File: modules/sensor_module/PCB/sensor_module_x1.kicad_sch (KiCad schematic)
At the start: 61 parts, among them J1 Screw_Terminal_01x02, J2 Conn_01x06_Socket, J3 Conn_01x03_Socket, SW1 SW_SPDT, U1 LM393, U2 MQ-5, U3 AMS1117-3.3, U4 AMS1117-5, U5 LM393, U6 DHT11, U7 ESP-12E, U8 PIR, U9 BISS0001

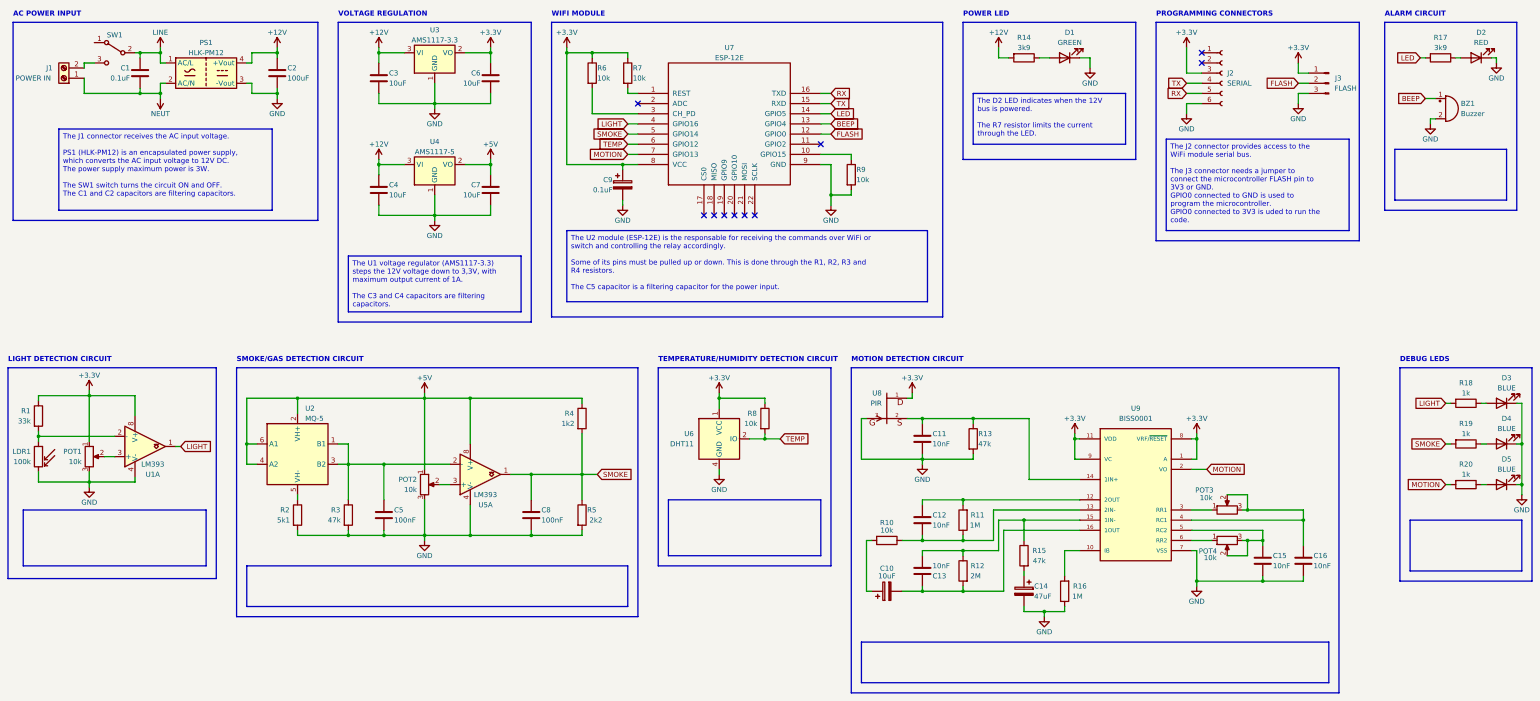
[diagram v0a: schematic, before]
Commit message: Sensor module PCB layout started
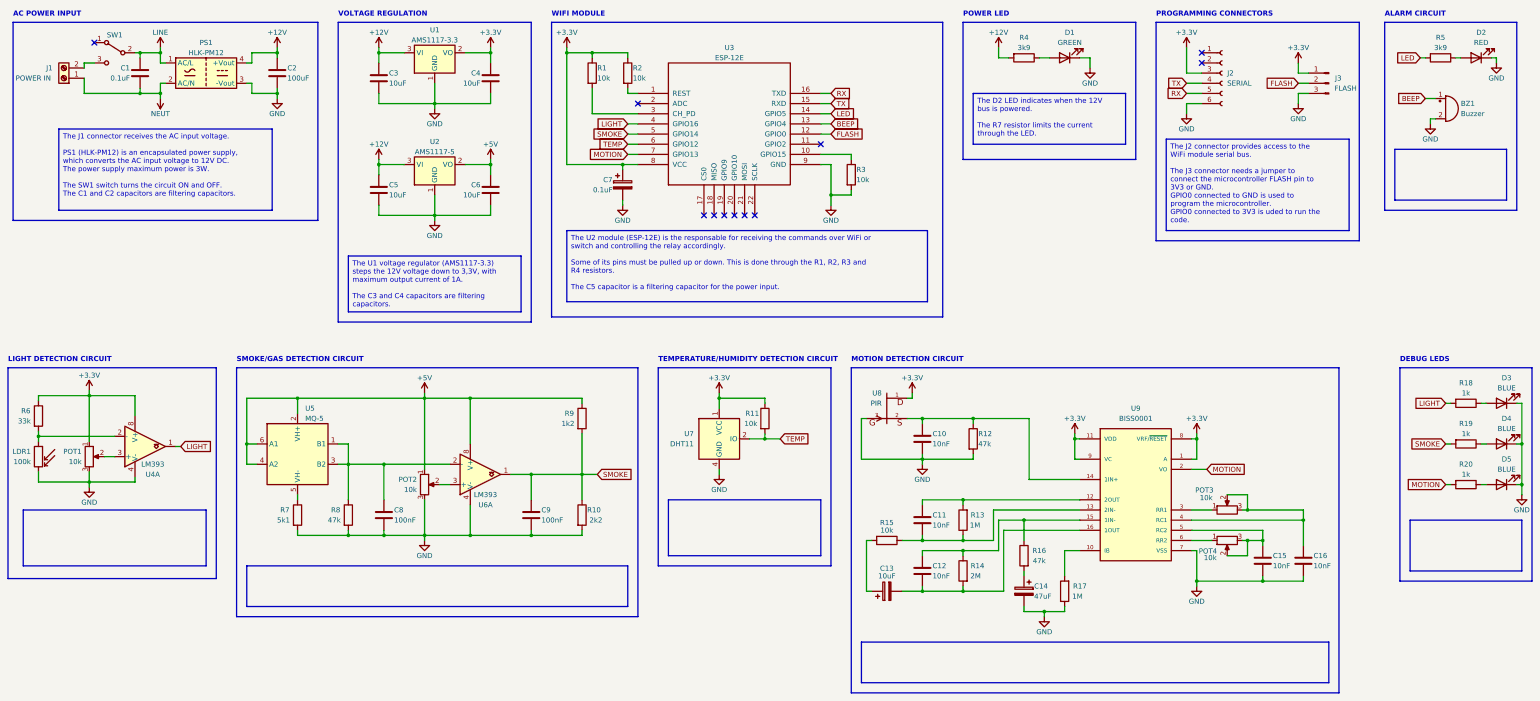
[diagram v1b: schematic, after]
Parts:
- removed U1, U5: LM393, symbol Comparator:LM393
- added U4, U6: LM393, Package_SO:SOIC-8-1EP_3.9x4.9mm_P1.27mm_EP2.62x3.51mm, symbol Comparator:LM393
- C10: renamed from C11; footprint (none) -> Capacitor_SMD:C_0603_1608Metric
- C11: renamed from C12; footprint (none) -> Capacitor_SMD:C_0603_1608Metric
- C12: renamed from C13; footprint (none) -> Capacitor_SMD:C_0603_1608Metric
- C13: renamed from C10; footprint (none) -> Capacitor_SMD:CP_Elec_5x5.4
- C14: footprint (none) -> Capacitor_SMD:CP_Elec_5x5.4
- C15, C16: footprint (none) -> Capacitor_SMD:C_0603_1608Metric
- C8: renamed from C5; footprint (none) -> Capacitor_SMD:C_0603_1608Metric
- C9: renamed from C8; footprint (none) -> Capacitor_SMD:C_0603_1608Metric
- POT1, POT2, POT3, POT4: footprint (none) -> Potentiometer_THT:Potentiometer_Bourns_3296W_Vertical
- U7: renamed from U6; footprint Sensor:Aosong_DHT11_5.5x12.0_P2.54mm -> MyLibrary:SNR4-2.54-15.5X12.0X5.5MM
- U8: footprint ZRE200GE:TO5 -> MyLibrary:TO5
- U9: footprint BISS0001:SOIC127P600X180-16N -> MyLibrary:SOIC127P600X180-16N
- renumbered C6 to C4, C4 to C5, C7 to C6, C9 to C7, R6 to R1, R5 to R10, R8 to R11, R13 to R12, R11 to R13, R12 to R14, R10 to R15, R15 to R16, R16 to R17, R7 to R2, R9 to R3, R14 to R4, R17 to R5, R1 to R6, R2 to R7, R3 to R8, R4 to R9, U3 to U1, U4 to U2, U7 to U3, U2 to U5
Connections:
- net +3.3V: now also U4.8 (V+)
- net +5V: now also U6.8 (V+)
- net GND: now also U4.4 (V-), U6.4 (V-)
- net LIGHT: now also U4.1
- net SMOKE: now also U6.1
- net at LDR1.1, R6.2: now also U4.2 (-)
- net at POT1.2: now also U4.3 (+)
- net at C8.1, R8.1, U5.1 (B1)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: now also U6.2 (-)
- net at POT2.2: now also U6.3 (+)
- no-connect marks 10 -> 11
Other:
- title: ON-OFF Module X1 -> Sensor Module
